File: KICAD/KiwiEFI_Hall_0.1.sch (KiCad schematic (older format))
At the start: 38 parts, among them J1 Conn_02x04_Counter_Clockwise, J2 ToolingHole, J3 ToolingHole, J4 ToolingHole, U1 SN74HC14N

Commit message: Update Schematic
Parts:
- D1, D4: value 1N5818-TP DO-41 or B130-13-F SMA -> B130-13-F SMA
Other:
- note added: "DEFAULT 1-2"
- note added: "DEFAULT \nCLOSED"
- note added: "DEFAULT \nOPEN"
- note added: "KiwiEfi HALL TRIGGER SENSOR CONDITIONER"
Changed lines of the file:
@@
 P 3095 4435
 F 0 "D4" H 3080 4540 50  0000 C CNN
-F 1 "1N5818-TP DO-41 or B130-13-F SMA" H 3110 4620 50  0000 C CNN
+F 1 "B130-13-F SMA" H 3110 4620 50  0000 C CNN
 F 2 "Diode_SMD:D_SMA_Handsoldering" H 3095 4435 50  0001 C CNN
 F 3 "~" H 3095 4435 50  0001 C CNN
@@
 P 2995 2285
 F 0 "D1" H 2985 2190 50  0000 C CNN
-F 1 "1N5818-TP DO-41 or B130-13-F SMA" H 3025 2120 50  0000 C CNN
+F 1 "B130-13-F SMA" H 3025 2120 50  0000 C CNN
 F 2 "Diode_SMD:D_SMA_Handsoldering" H 2995 2285 50  0001 C CNN
 F 3 "~" H 2995 2285 50  0001 C CNN
@@
 NoConn ~ 5820 7095
 NoConn ~ 5835 7330
+Text Notes 7160 6890 0    118  ~ 24
+KiwiEfi HALL TRIGGER SENSOR CONDITIONER
+Text Notes 7770 5590 0    50   ~ 0
+DEFAULT 1-2
+Text Notes 8890 5590 0    50   ~ 0
+DEFAULT 1-2
+Text Notes 3325 3360 0    50   ~ 0
+DEFAULT \nCLOSED
+Text Notes 2250 3375 0    50   ~ 0
+DEFAULT \nOPEN
+Text Notes 2475 5530 0    50   ~ 0
+DEFAULT \nOPEN
+Text Notes 3375 5525 0    50   ~ 0
+DEFAULT \nCLOSED
+Text Notes 3845 5520 0    50   ~ 0
+DEFAULT \nCLOSED
+Text Notes 3810 3355 0    50   ~ 0
+DEFAULT \nCLOSED
 $EndSCHEMATC

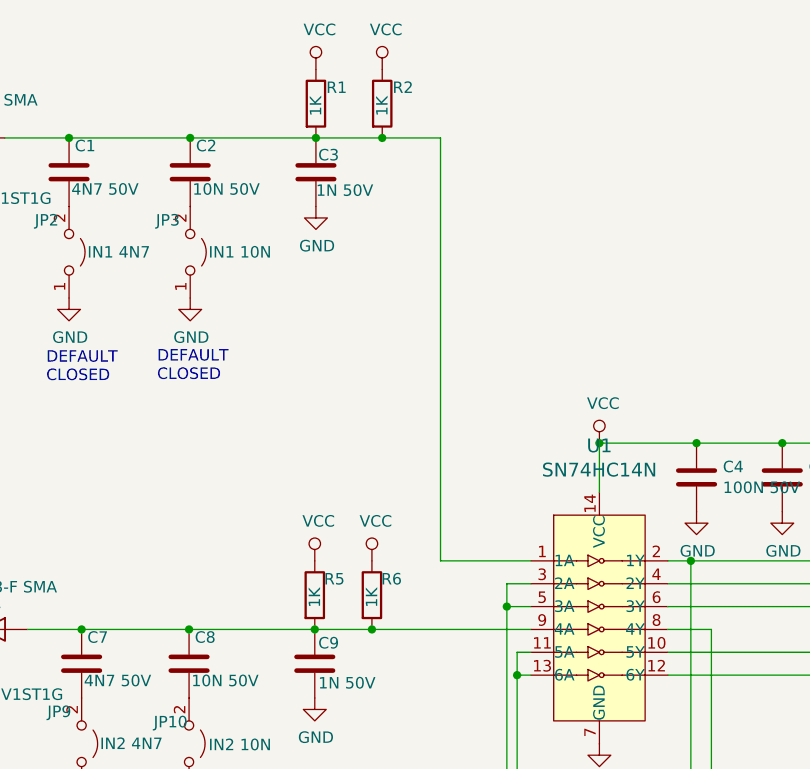
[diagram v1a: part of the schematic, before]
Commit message: Doccumenting optional components
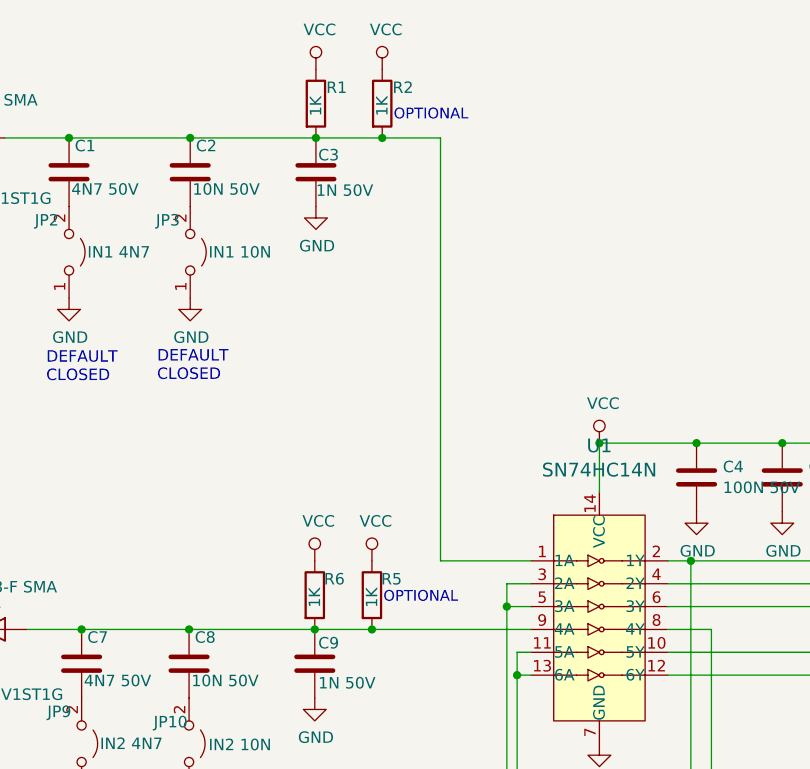
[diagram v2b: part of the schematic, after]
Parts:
- renumbered R6 to R5, R5 to R6
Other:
- note added: "OPTIONAL"
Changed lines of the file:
@@
 $EndDescr
 $Comp
-L Device:R R5
+L Device:R R6
 U 1 1 5FDC308F
 P 4500 4285
-F 0 "R5" H 4540 4355 50  0000 L CNN
+F 0 "R6" H 4540 4355 50  0000 L CNN
 F 1 "1K" V 4500 4230 50  0000 L CNN
 F 2 "Resistor_SMD:R_0805_2012Metric_Pad1.15x1.40mm_HandSolder" V 4430 4285 50  0001 C CNN
@@
 	4795 2285 5050 2285
 $Comp
-L Device:R R6
+L Device:R R5
 U 1 1 604DCEF4
 P 4750 4285
-F 0 "R6" H 4790 4355 50  0000 L CNN
+F 0 "R5" H 4790 4355 50  0000 L CNN
 F 1 "1K" V 4750 4230 50  0000 L CNN
 F 2 "Resistor_SMD:R_0805_2012Metric_Pad1.15x1.40mm_HandSolder" V 4680 4285 50  0001 C CNN
@@
 Text Notes 3810 3355 0    50   ~ 0
 DEFAULT \nCLOSED
+Text Notes 4845 2215 0    47   ~ 0
+OPTIONAL
+Text Notes 4800 4325 0    47   ~ 0
+OPTIONAL
 $EndSCHEMATC
